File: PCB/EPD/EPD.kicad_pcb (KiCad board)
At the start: 2 copper layers, 70 x 70 mm, 68 parts, among them J1 Conn_01x26, J2 Shelly, J3 USB-PROG, J4 BTN1, J6 BTN2, J7 USB-C-Socket-V, J8 PWR, P1 +, P10 2, P11 1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

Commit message: Updated
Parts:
- removed C13, C16: 1uF 50V, RevK:C_0402
- C11, C7: value 1uF 50V -> 1uF 10V
- C12, C15, C3, C4: value 1uF 50V -> 1uF 25V
- C14: value 100nF 50V -> 1uF 25V
- C18: value 10uF -> 4.7uF
- D1, D2, D3: value 1N5819W -> MBR0530
- L1: value 68uH -> 10uH; footprint RevK:L_0805 -> RevK:L_4x4
- Q1: value DMG1012T -> BSS138; footprint RevK:SOT-323_SC-70-3 -> RevK:SOT-23
- R2: value 10K -> 3R
- R8: value 3R -> 10K
- moved D4 20.6 mm to (93.2, 79.6)
- moved Q1 11.6 mm to (111.7, 74.2), turned to 90 degrees
- moved R8 9.89 mm to (95.6, 80.0), turned to 90 degrees
- moved C18 8.47 mm to (108.7, 82.8), turned to 0 degrees
- moved C15 7.70 mm to (105.1, 80.0)
- moved C12 7.20 mm to (96.5, 80.0)
- moved R2 6.84 mm to (89.5, 76.9), turned to 180 degrees
- moved C14 6.80 mm to (106.9, 80.0)
- moved R1 3.80 mm to (89.5, 78.5), turned to 0 degrees
- moved D3 3.80 mm to (111.4, 77.2)
- moved C17 3.70 mm to (111.1, 82.8), turned to 180 degrees
- moved C4 2.20 mm to (104.2, 80.0)
- moved C7 2.20 mm to (103.3, 80.0)
- moved C11 2.20 mm to (102.4, 80.0)
- moved L1 1.86 mm to (110.3, 85.5), turned to 180 degrees
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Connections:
- C11 pad 1: Net-(J1-Pin_20) -> +3.3V
- C12 pad 1: Net-(J1-Pin_19) -> Net-(J1-Pin_5)
- C14 pad 1: +3.3V -> Net-(D2-A)
- C15 pad 1: Net-(J1-Pin_5) -> Net-(D3-K)
- C17 pad 1: Net-(D2-A) -> Net-(D3-A)
- C17 pad 2: Net-(D1-K) -> Net-(D1-A)
- C3 pad 1: Net-(D1-A) -> Net-(J1-Pin_22)
- C4 pad 1: Net-(J1-Pin_22) -> Net-(J1-Pin_20)
- C7 pad 1: Net-(D2-K) -> Net-(J1-Pin_18)
- D1 pad 1: Net-(D1-K) -> GND
- D2 pad 1: Net-(D2-K) -> Net-(D1-A)
- D3 pad 1: GND -> Net-(D3-K)
- D3 pad 2: Net-(D1-K) -> Net-(D3-A)
- J1 pad 21: Net-(D2-K) -> Net-(D3-K)
- J1 pad 23: Net-(D1-A) -> Net-(D2-A)
- JP1 pad 1: GND -> Net-(JP1-A)
- JP1 pad 2: Net-(J1-Pin_8) -> Net-(J1-Pin_3)
- JP1 pad 3: +3.3V -> Net-(JP1-B)
- JP2 pad 1: Net-(JP2-A) -> GND
- JP2 pad 2: Net-(J1-Pin_3) -> Net-(J1-Pin_8)
- JP2 pad 3: Net-(JP2-B) -> +3.3V
- L1 pad 1: Net-(D2-A) -> Net-(D3-A)
- Q1 pad 3: Net-(D2-A) -> Net-(D3-A)
- R1 pad 1: Net-(JP2-A) -> Net-(JP1-A)
- R2 pad 2: Net-(J1-Pin_2) -> Net-(JP1-B)
- R8 pad 2: Net-(JP2-B) -> Net-(J1-Pin_2)
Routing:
- net Net-(D2-K): track 14.3 -> 0.00 mm, vias 2 -> 0
- net Net-(D3-A): track 0.00 -> 14.0 mm
- net Net-(D3-K): track 0.00 -> 12.3 mm, vias 0 -> 2
- net RGB: track 26.2 -> 15.2 mm
- net Net-(D1-K): track 9.98 -> 0.00 mm
- net GND: track 35.5 -> 27.0 mm
- net +3.3V: track 102.8 -> 97.5 mm
- net Net-(D2-A): track 6.64 -> 10.6 mm
- net Net-(J1-Pin_19): track 2.34 -> 0.00 mm
- net Net-(J1-Pin_2): track 17.8 -> 20.1 mm
- net Net-(J1-Pin_4): track 2.26 -> 0.00 mm
- net Net-(JP1-A): track 0.00 -> 1.86 mm
- net Net-(JP2-B): track 1.60 -> 0.00 mm
- net Net-(JP2-A): track 1.60 -> 0.00 mm
- net Net-(JP1-B): track 0.00 -> 1.54 mm
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
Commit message: Tidy
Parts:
- C1: footprint RevK:C_0402 -> RevK:C_0603
- C11, C7: value 1uF 10V -> 1uF
- C12, C14, C15, C3, C4: value 1uF 25V -> 1uF
- D6: value D -> MBR0530
- moved C1 0.36 mm to (108.0, 79.7)

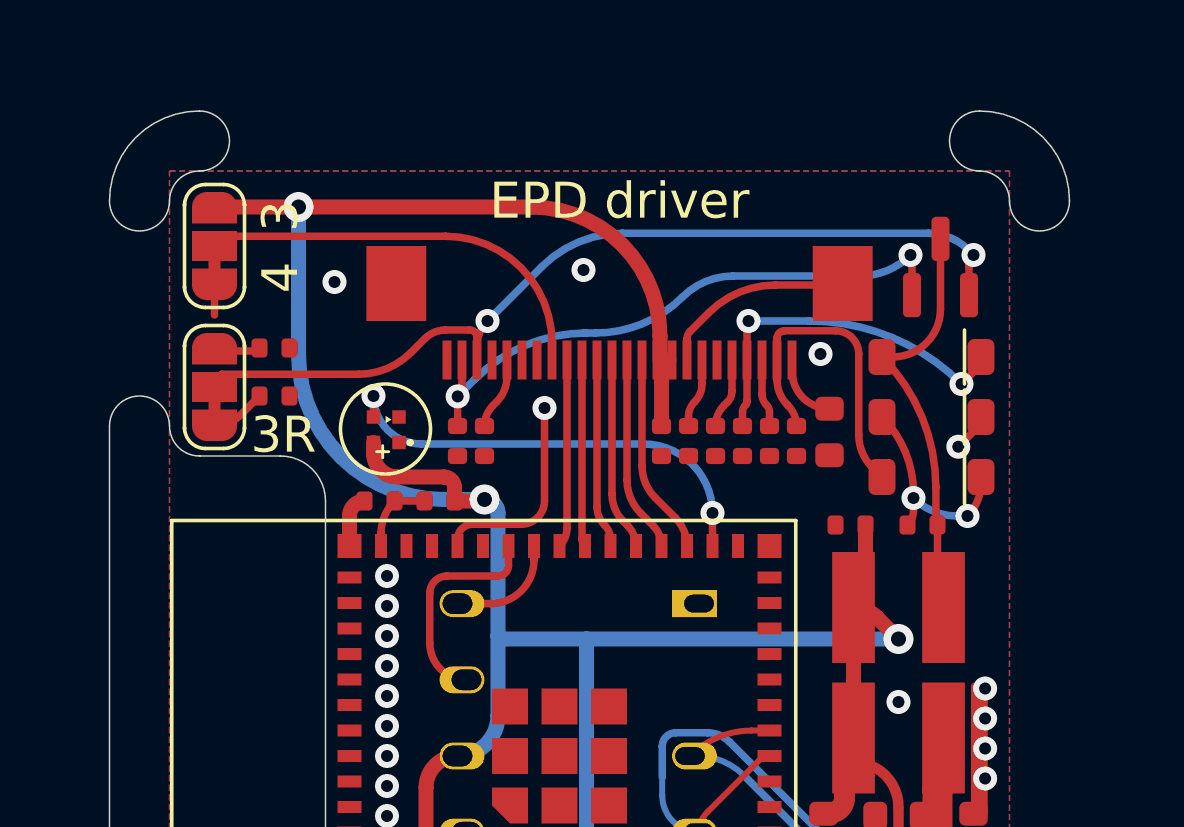
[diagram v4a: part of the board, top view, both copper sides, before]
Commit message: Updated so RESE is cleaner
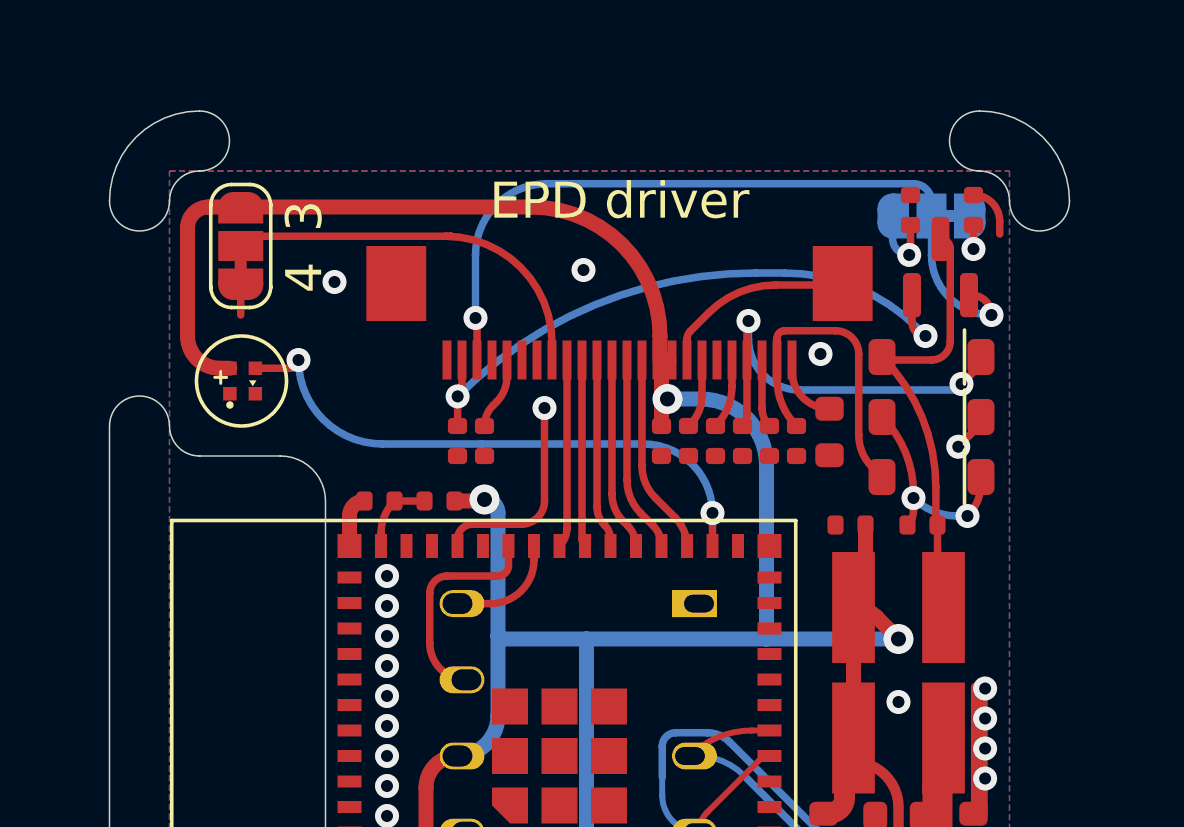
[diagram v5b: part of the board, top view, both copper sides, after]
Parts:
- JP1: moved to B.Cu
- moved JP1 24.6 mm to (111.4, 72.5), turned to 180 degrees
- moved R1 24.1 mm to (112.8, 72.3), turned to 90 degrees
- moved R2 21.7 mm to (110.7, 72.3), turned to -90 degrees
- moved D4 5.06 mm to (88.4, 78.0), turned to 90 degrees
- moved JP2 0.88 mm to (88.4, 73.5)
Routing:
- net Net-(J1-Pin_3): track 30.6 -> 26.2 mm
- net RGB: track 15.2 -> 19.2 mm
- net GND: track 27.0 -> 28.7 mm
- net Net-(D3-A): track 14.0 -> 15.1 mm
- net Net-(D3-K): track 12.3 -> 13.4 mm
- net Net-(JP1-B): track 1.54 -> 2.61 mm, vias 0 -> 1
- net Net-(J1-Pin_2): track 20.1 -> 21.0 mm
- net Net-(J1-Pin_8): track 13.9 -> 13.2 mm
- net Net-(JP1-A): track 1.86 -> 1.94 mm, vias 0 -> 1
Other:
- board text added: "3R/0R47"
- board text removed: "3R"

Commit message: Tidy
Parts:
- C12, C14, C15, C3, C4: value 1uF -> 1uF 25V
- moved R8 16.2 mm to (109.8, 72.3), turned to -90 degrees
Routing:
- net Net-(J1-Pin_2): track 21.0 -> 22.7 mm
- net +3.3V: track 97.0 -> 96.0 mm
- net Net-(D3-A): track 15.1 -> 14.4 mm
- net Net-(J1-Pin_3): track 26.2 -> 25.7 mm
- net Net-(J1-Pin_8): track 13.2 -> 12.7 mm
- net GND: track 28.7 -> 28.3 mm, vias 26 -> 29
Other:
- board text added: "+"
- board text added: "-"

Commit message: Tidy
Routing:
- net GND: vias 29 -> 28
